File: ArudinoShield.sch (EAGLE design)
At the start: 27 parts, among them IC1 L298, IC3 REG1117

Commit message: renamed component, updated ignore
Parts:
- renumbered IC3 to VREG
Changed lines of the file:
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@@
 <part name="J6" library="con-amp" library_urn="urn:adsk.eagle:library:127" deviceset="MTA03-100" device="" package3d_urn="urn:adsk.eagle:package:8081621/1"/>
 <part name="JP1" library="jumper" library_urn="urn:adsk.eagle:library:252" deviceset="JP1E" device="" package3d_urn="urn:adsk.eagle:package:15455/1"/>
-<part name="IC3" library="burr-brown" library_urn="urn:adsk.eagle:library:111" deviceset="REG1117" device="" package3d_urn="urn:adsk.eagle:package:4940/1"/>
+<part name="VREG" library="burr-brown" library_urn="urn:adsk.eagle:library:111" deviceset="REG1117" device="" package3d_urn="urn:adsk.eagle:package:4940/1"/>
 </parts>
 <sheets>
@@
 <attribute name="VALUE" x="210.82" y="-13.335" size="1.778" layer="96"/>
 </instance>
-<instance part="IC3" gate="G$1" x="139.7" y="12.7" smashed="yes">
+<instance part="VREG" gate="G$1" x="139.7" y="12.7" smashed="yes">
 <attribute name="NAME" x="132.08" y="18.415" size="1.778" layer="95" ratio="10"/>
 <attribute name="VALUE" x="134.62" y="15.24" size="1.778" layer="96" ratio="10"/>
@@
 <pinref part="JP1" gate="A" pin="2"/>
 <wire x1="208.28" y1="-12.7" x2="208.28" y2="-10.16" width="0.1524" layer="91"/>
-<pinref part="IC3" gate="G$1" pin="VOUT"/>
+<pinref part="VREG" gate="G$1" pin="VOUT"/>
 </segment>
 </net>
@@
 <segment>
 <pinref part="J2" gate="G$1" pin="2"/>
-<pinref part="IC3" gate="G$1" pin="VIN"/>
+<pinref part="VREG" gate="G$1" pin="VIN"/>
 <wire x1="127" y1="12.7" x2="121.92" y2="12.7" width="0.1524" layer="91"/>
 </segment>
@@
 <wire x1="175.26" y1="30.48" x2="175.26" y2="-12.7" width="0.1524" layer="91"/>
 <junction x="175.26" y="-12.7"/>
-<pinref part="IC3" gate="G$1" pin="GND"/>
-</segment>
-</net>
+<pinref part="VREG" gate="G$1" pin="GND"/>
+</segment>
+</net>

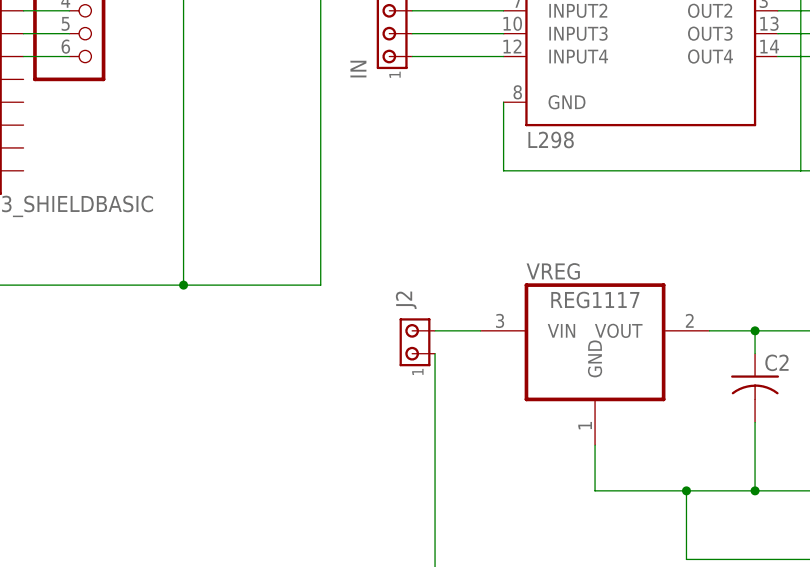
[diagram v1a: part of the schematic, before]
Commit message: added routes to board
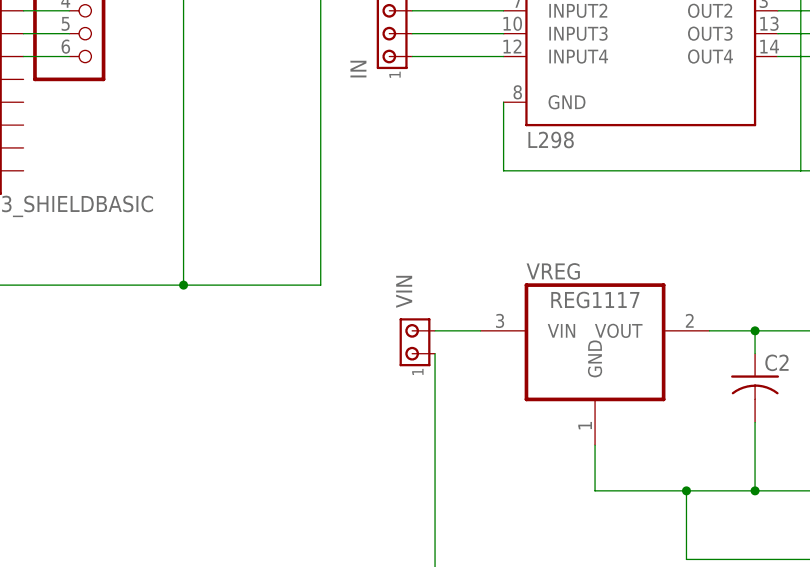
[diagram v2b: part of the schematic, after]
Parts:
- renumbered J2 to VIN
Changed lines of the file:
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@@
 <part name="D8" library="diode" library_urn="urn:adsk.eagle:library:210" deviceset="1N4004" device="" package3d_urn="urn:adsk.eagle:package:43336/1"/>
 <part name="EN" library="con-amp" library_urn="urn:adsk.eagle:library:127" deviceset="MTA02-156" device="" package3d_urn="urn:adsk.eagle:package:8081562/1"/>
-<part name="J2" library="con-amp" library_urn="urn:adsk.eagle:library:127" deviceset="MTA02-156" device="" package3d_urn="urn:adsk.eagle:package:8081562/1"/>
+<part name="VIN" library="con-amp" library_urn="urn:adsk.eagle:library:127" deviceset="MTA02-156" device="" package3d_urn="urn:adsk.eagle:package:8081562/1"/>
 <part name="OUT1" library="con-amp" library_urn="urn:adsk.eagle:library:127" deviceset="MTA02-156" device="" package3d_urn="urn:adsk.eagle:package:8081562/1"/>
 <part name="OUT2" library="con-amp" library_urn="urn:adsk.eagle:library:127" deviceset="MTA02-156" device="" package3d_urn="urn:adsk.eagle:package:8081562/1"/>
@@
 <attribute name="VALUE" x="120.65" y="60.96" size="1.778" layer="96" rot="R90"/>
 </instance>
-<instance part="J2" gate="G$1" x="119.38" y="10.16" smashed="yes" rot="R90">
+<instance part="VIN" gate="G$1" x="119.38" y="10.16" smashed="yes" rot="R90">
 <attribute name="NAME" x="119.38" y="15.24" size="1.778" layer="95" rot="R90"/>
 <attribute name="VALUE" x="123.19" y="15.24" size="1.778" layer="96" rot="R90"/>
@@
 <net name="N$27" class="0">
 <segment>
-<pinref part="J2" gate="G$1" pin="2"/>
+<pinref part="VIN" gate="G$1" pin="2"/>
 <pinref part="VREG" gate="G$1" pin="VIN"/>
 <wire x1="127" y1="12.7" x2="121.92" y2="12.7" width="0.1524" layer="91"/>
@@
 <pinref part="J6" gate="G$1" pin="1"/>
 <wire x1="198.12" y1="-15.24" x2="198.12" y2="-22.86" width="0.1524" layer="91"/>
-<pinref part="J2" gate="G$1" pin="1"/>
+<pinref part="VIN" gate="G$1" pin="1"/>
 <wire x1="198.12" y1="-22.86" x2="121.92" y2="-22.86" width="0.1524" layer="91"/>
 <wire x1="121.92" y1="-22.86" x2="121.92" y2="10.16" width="0.1524" layer="91"/>

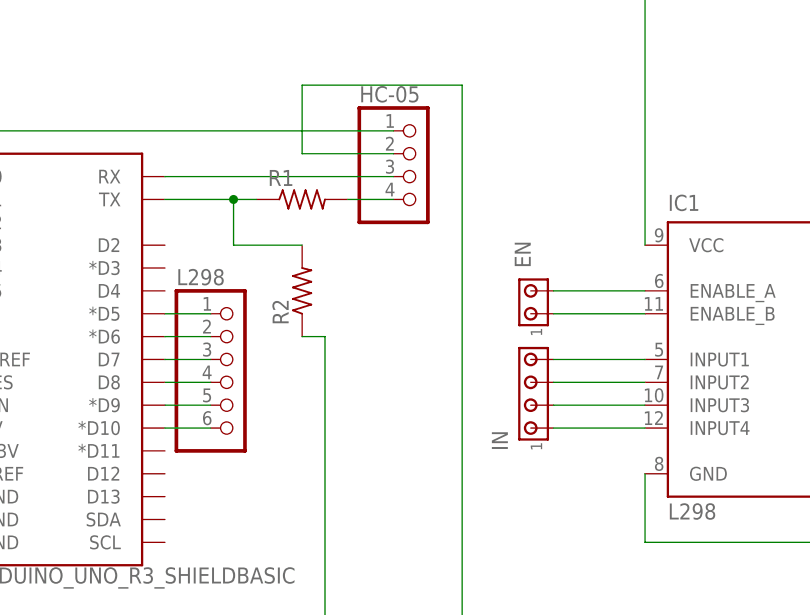
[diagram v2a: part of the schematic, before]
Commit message: reduced schematic
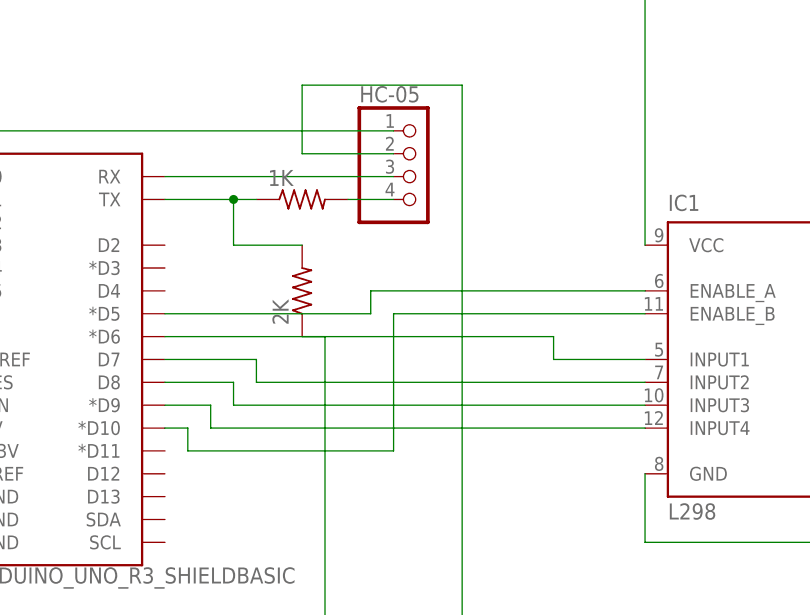
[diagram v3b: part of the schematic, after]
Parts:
- removed EN: (no value), con-amp:MTA02-156
- removed IN: (no value), con-amp:MTA04-156
- removed L298: (no value), adafruit:PINHD-1X6
- renumbered R1 to 1K, R2 to 2K
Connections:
- removed net N$19: EN.2, IC1.ENABLE_A
- removed net N$23: IC1.INPUT3, IN.2
- removed net N$3: B1.D7, L298.3
- removed net N$4: B1.D8, L298.4
- removed net N$5: B1.*D9, L298.5
- removed net N$6: B1.*D10, L298.6
- net N$1: now also IC1.ENABLE_A; no longer L298.1
- net N$2: now also B1.D8, IC1.INPUT3; no longer B1.*D6, L298.2
- net N$20: now also B1.*D10; no longer EN.1
- net N$21: now also B1.*D6; no longer IN.4
- net N$22: now also B1.D7; no longer IN.3
- net N$24: now also B1.*D9; no longer IN.1

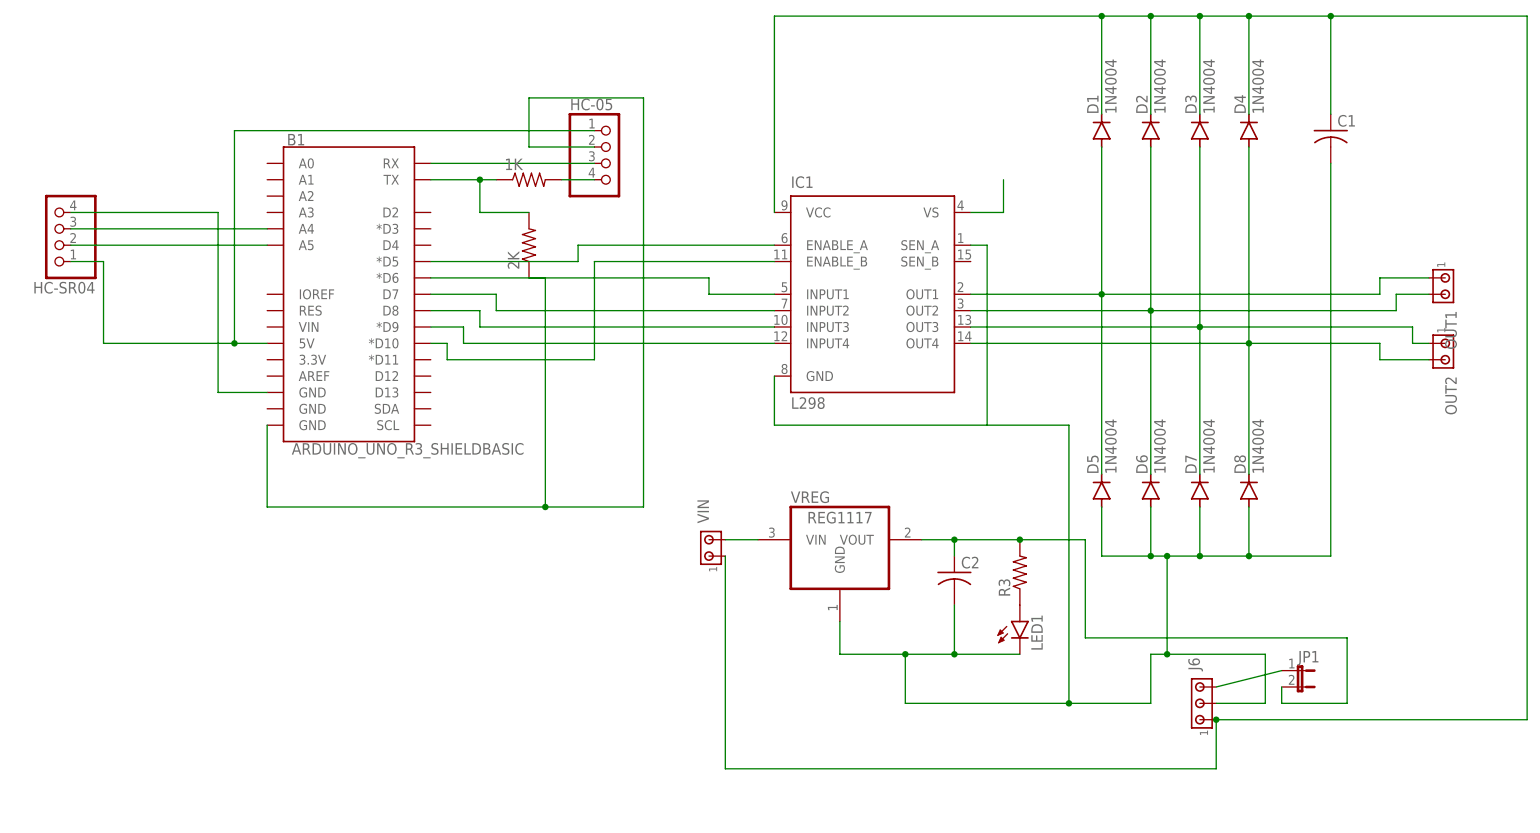
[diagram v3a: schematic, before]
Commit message: Reduced shield schematic
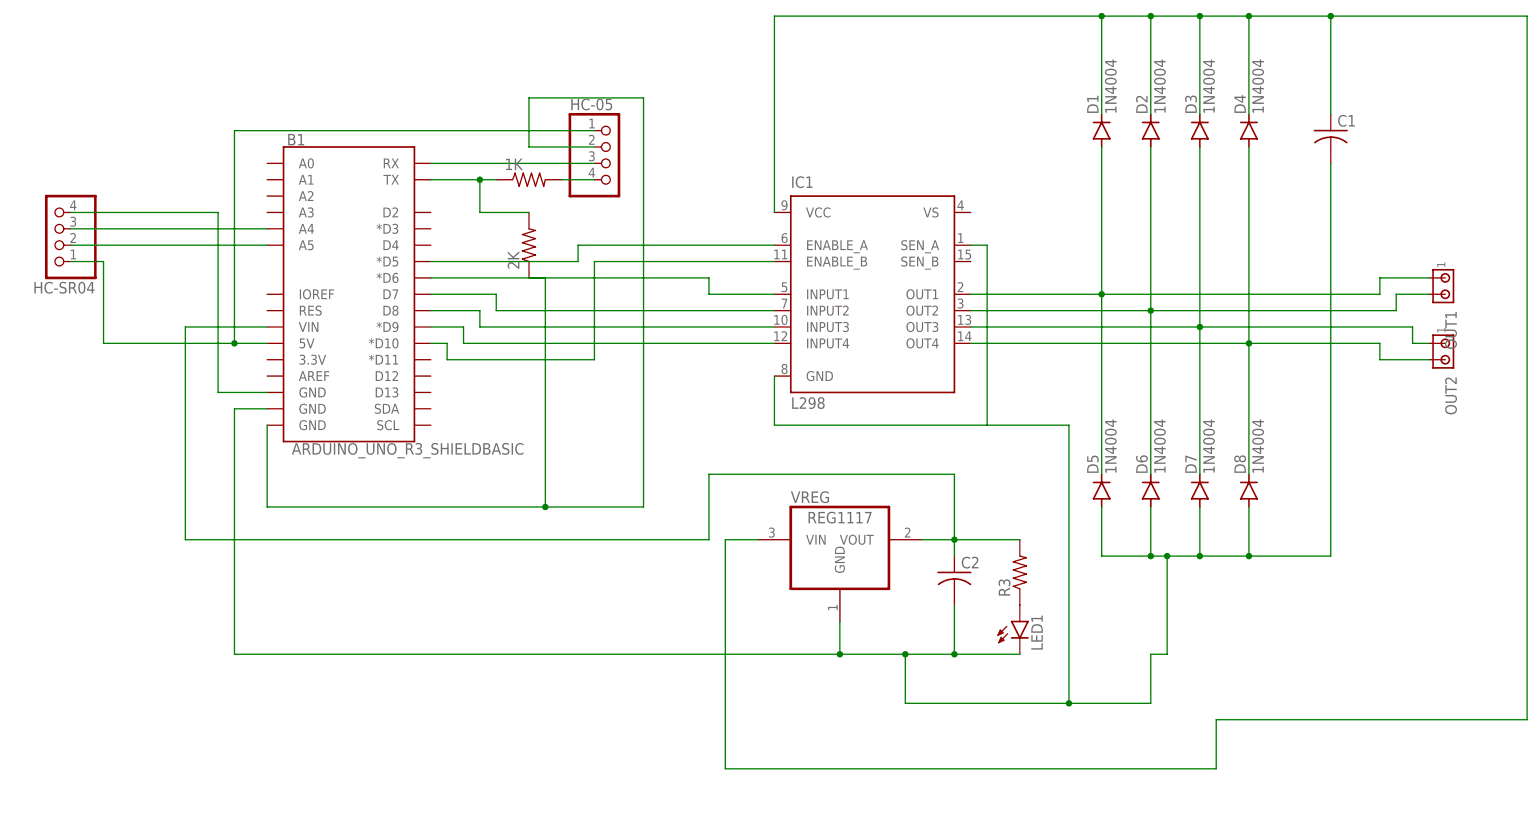
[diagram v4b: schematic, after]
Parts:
- removed J6: (no value), con-amp:MTA03-100
- removed JP1: (no value), jumper:JP1E
- removed VIN: (no value), con-amp:MTA02-156
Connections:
- removed net N$27: VIN.2, VREG.VIN
- removed net N$28: IC1.VS
- removed net N$30: J6.3, JP1.1
- net N$26: now also B1.VIN; no longer JP1.2
- net N$29: now also B1.GND@1; no longer J6.2
- net N$31: now also VREG.VIN; no longer J6.1, VIN.1
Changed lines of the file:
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@@
 <part name="D7" library="diode" library_urn="urn:adsk.eagle:library:210" deviceset="1N4004" device="" package3d_urn="urn:adsk.eagle:package:43336/1"/>
 <part name="D8" library="diode" library_urn="urn:adsk.eagle:library:210" deviceset="1N4004" device="" package3d_urn="urn:adsk.eagle:package:43336/1"/>
-<part name="VIN" library="con-amp" library_urn="urn:adsk.eagle:library:127" deviceset="MTA02-156" device="" package3d_urn="urn:adsk.eagle:package:8081562/1"/>
 <part name="OUT1" library="con-amp" library_urn="urn:adsk.eagle:library:127" deviceset="MTA02-156" device="" package3d_urn="urn:adsk.eagle:package:8081562/1"/>
 <part name="OUT2" library="con-amp" library_urn="urn:adsk.eagle:library:127" deviceset="MTA02-156" device="" package3d_urn="urn:adsk.eagle:package:8081562/1"/>
@@
 <part name="R3" library="rcl" library_urn="urn:adsk.eagle:library:334" deviceset="R-US_" device="0207/10" package3d_urn="urn:adsk.eagle:package:23491/2"/>
 <part name="LED1" library="led" library_urn="urn:adsk.eagle:library:259" deviceset="LED" device="5MM" package3d_urn="urn:adsk.eagle:package:15799/2"/>
-<part name="J6" library="con-amp" library_urn="urn:adsk.eagle:library:127" deviceset="MTA03-100" device="" package3d_urn="urn:adsk.eagle:package:8081621/1"/>
-<part name="JP1" library="jumper" library_urn="urn:adsk.eagle:library:252" deviceset="JP1E" device="" package3d_urn="urn:adsk.eagle:package:15455/1"/>
 <part name="VREG" library="burr-brown" library_urn="urn:adsk.eagle:library:111" deviceset="REG1117" device="" package3d_urn="urn:adsk.eagle:package:4940/1"/>
 </parts>
@@
 <attribute name="VALUE" x="205.5114" y="22.86" size="1.778" layer="96" rot="R90"/>
 </instance>
-<instance part="VIN" gate="G$1" x="119.38" y="10.16" smashed="yes" rot="R90">
-<attribute name="NAME" x="119.38" y="15.24" size="1.778" layer="95" rot="R90"/>
-<attribute name="VALUE" x="123.19" y="15.24" size="1.778" layer="96" rot="R90"/>
-</instance>
 <instance part="OUT1" gate="G$1" x="233.68" y="53.34" smashed="yes" rot="R270">
 <attribute name="NAME" x="233.68" y="48.26" size="1.778" layer="95" rot="R270"/>
@@
 <attribute name="NAME" x="171.196" y="-4.572" size="1.778" layer="95" rot="R90"/>
 <attribute name="VALUE" x="173.355" y="-4.572" size="1.778" layer="96" rot="R90"/>
-</instance>
-<instance part="J6" gate="G$1" x="195.58" y="-12.7" smashed="yes" rot="R90">
-<attribute name="NAME" x="195.58" y="-7.62" size="1.778" layer="95" rot="R90"/>
-<attribute name="VALUE" x="199.39" y="-7.62" size="1.778" layer="96" rot="R90"/>
-</instance>
-<instance part="JP1" gate="A" x="210.82" y="-7.62" smashed="yes" rot="R270">
-<attribute name="NAME" x="210.82" y="-6.35" size="1.778" layer="95"/>
-<attribute name="VALUE" x="210.82" y="-13.335" size="1.778" layer="96"/>
 </instance>
 <instance part="VREG" gate="G$1" x="139.7" y="12.7" smashed="yes">
@@
 <wire x1="157.48" y1="10.16" x2="157.48" y2="12.7" width="0.1524" layer="91"/>
 <junction x="157.48" y="12.7"/>
-<wire x1="167.64" y1="12.7" x2="177.8" y2="12.7" width="0.1524" layer="91"/>
-<junction x="167.64" y="12.7"/>
-<wire x1="177.8" y1="12.7" x2="177.8" y2="-2.54" width="0.1524" layer="91"/>
-<wire x1="177.8" y1="-2.54" x2="218.44" y2="-2.54" width="0.1524" layer="91"/>
-<wire x1="218.44" y1="-2.54" x2="218.44" y2="-12.7" width="0.1524" layer="91"/>
-<wire x1="218.44" y1="-12.7" x2="208.28" y2="-12.7" width="0.1524" layer="91"/>
-<pinref part="JP1" gate="A" pin="2"/>
-<wire x1="208.28" y1="-12.7" x2="208.28" y2="-10.16" width="0.1524" layer="91"/>
 <pinref part="VREG" gate="G$1" pin="VOUT"/>
-</segment>
-</net>
-<net name="N$27" class="0">
-<segment>
-<pinref part="VIN" gate="G$1" pin="2"/>
-<pinref part="VREG" gate="G$1" pin="VIN"/>
-<wire x1="127" y1="12.7" x2="121.92" y2="12.7" width="0.1524" layer="91"/>
-</segment>
-</net>
-<net name="N$28" class="0">
-<segment>
-<pinref part="IC1" gate="L298" pin="VS"/>
-<wire x1="160.02" y1="63.5" x2="165.1" y2="63.5" width="0.1524" layer="91"/>
-<wire x1="165.1" y1="63.5" x2="165.1" y2="68.58" width="0.1524" layer="91"/>
+<pinref part="B1" gate="G$1" pin="VIN"/>
+<wire x1="50.8" y1="45.72" x2="38.1" y2="45.72" width="0.1524" layer="91"/>
+<wire x1="38.1" y1="45.72" x2="38.1" y2="12.7" width="0.1524" layer="91"/>
+<wire x1="38.1" y1="12.7" x2="119.38" y2="12.7" width="0.1524" layer="91"/>
+<wire x1="119.38" y1="12.7" x2="119.38" y2="22.86" width="0.1524" layer="91"/>
+<wire x1="119.38" y1="22.86" x2="157.48" y2="22.86" width="0.1524" layer="91"/>
+<wire x1="157.48" y1="22.86" x2="157.48" y2="12.7" width="0.1524" layer="91"/>
 </segment>
 </net>
@@
 <wire x1="175.26" y1="-12.7" x2="187.96" y2="-12.7" width="0.1524" layer="91"/>
 <wire x1="187.96" y1="-12.7" x2="187.96" y2="-5.08" width="0.1524" layer="91"/>
-<pinref part="J6" gate="G$1" pin="2"/>
-<wire x1="198.12" y1="-12.7" x2="205.74" y2="-12.7" width="0.1524" layer="91"/>
 <wire x1="187.96" y1="-5.08" x2="190.5" y2="-5.08" width="0.1524" layer="91"/>
-<wire x1="190.5" y1="-5.08" x2="205.74" y2="-5.08" width="0.1524" layer="91"/>
-<wire x1="205.74" y1="-5.08" x2="205.74" y2="-12.7" width="0.1524" layer="91"/>
 <pinref part="D5" gate="1" pin="A"/>
 <wire x1="180.34" y1="17.78" x2="180.34" y2="10.16" width="0.1524" layer="91"/>
@@
 <junction x="203.2" y="10.16"/>
 <wire x1="190.5" y1="-5.08" x2="190.5" y2="10.16" width="0.1524" layer="91"/>
-<junction x="190.5" y="-5.08"/>
 <junction x="190.5" y="10.16"/>
 <wire x1="162.56" y1="30.48" x2="175.26" y2="30.48" width="0.1524" layer="91"/>
@@
 <junction x="175.26" y="-12.7"/>
 <pinref part="VREG" gate="G$1" pin="GND"/>
-</segment>
-</net>
-<net name="N$30" class="0">
-<segment>
-<pinref part="J6" gate="G$1" pin="3"/>
-<pinref part="JP1" gate="A" pin="1"/>
-<wire x1="198.12" y1="-10.16" x2="208.28" y2="-7.62" width="0.1524" layer="91"/>
+<pinref part="B1" gate="G$1" pin="GND@1"/>
+<wire x1="50.8" y1="33.02" x2="45.72" y2="33.02" width="0.1524" layer="91"/>
+<wire x1="45.72" y1="33.02" x2="45.72" y2="-5.08" width="0.1524" layer="91"/>
+<wire x1="45.72" y1="-5.08" x2="139.7" y2="-5.08" width="0.1524" layer="91"/>
+<junction x="139.7" y="-5.08"/>
 </segment>
 </net>
 <net name="N$31" class="0">
 <segment>
-<pinref part="J6" gate="G$1" pin="1"/>
 <wire x1="198.12" y1="-15.24" x2="198.12" y2="-22.86" width="0.1524" layer="91"/>
-<pinref part="VIN" gate="G$1" pin="1"/>
 <wire x1="198.12" y1="-22.86" x2="121.92" y2="-22.86" width="0.1524" layer="91"/>
-<wire x1="121.92" y1="-22.86" x2="121.92" y2="10.16" width="0.1524" layer="91"/>
+<wire x1="121.92" y1="-22.86" x2="121.92" y2="12.7" width="0.1524" layer="91"/>
 <wire x1="198.12" y1="-15.24" x2="246.38" y2="-15.24" width="0.1524" layer="91"/>
-<junction x="198.12" y="-15.24"/>
 <pinref part="D1" gate="1" pin="C"/>
 <wire x1="180.34" y1="78.74" x2="180.34" y2="93.98" width="0.1524" layer="91"/>
@@
 <wire x1="246.38" y1="93.98" x2="215.9" y2="93.98" width="0.1524" layer="91"/>
 <junction x="215.9" y="93.98"/>
-</segment>
-</net>
+<pinref part="VREG" gate="G$1" pin="VIN"/>
+<wire x1="127" y1="12.7" x2="121.92" y2="12.7" width="0.1524" layer="91"/>
+</segment>
+</net>
